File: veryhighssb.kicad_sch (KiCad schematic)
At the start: 1 part, among them U1 STM32WL33CCV6TR

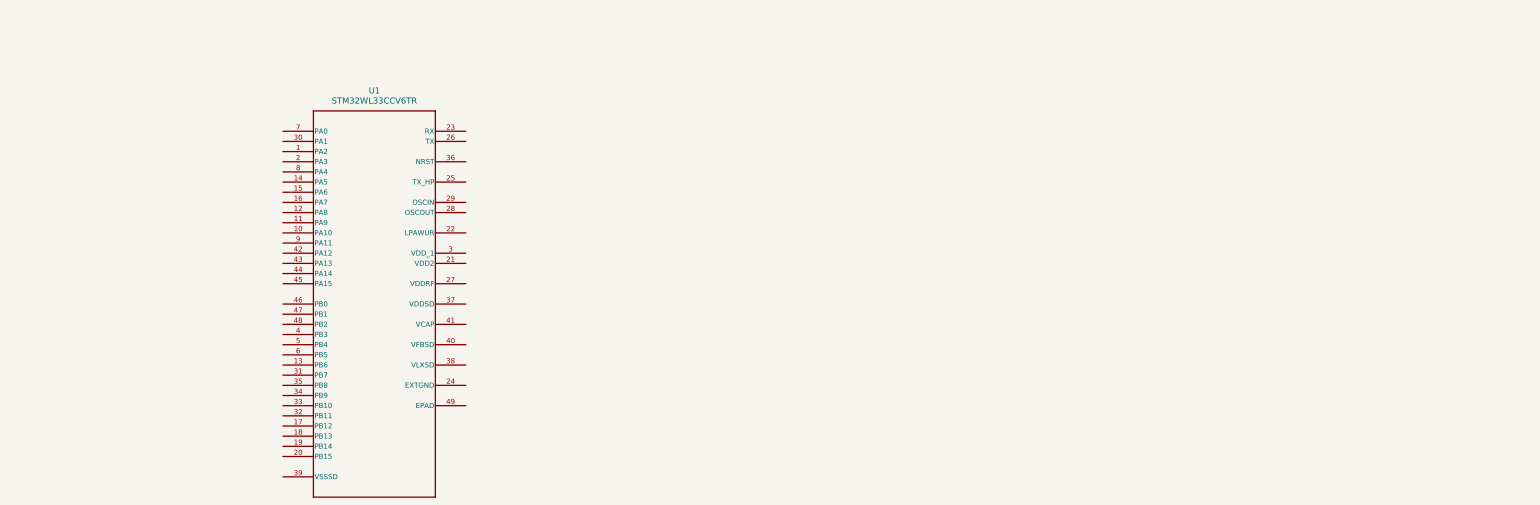
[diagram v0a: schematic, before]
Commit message: Added mcu, swd
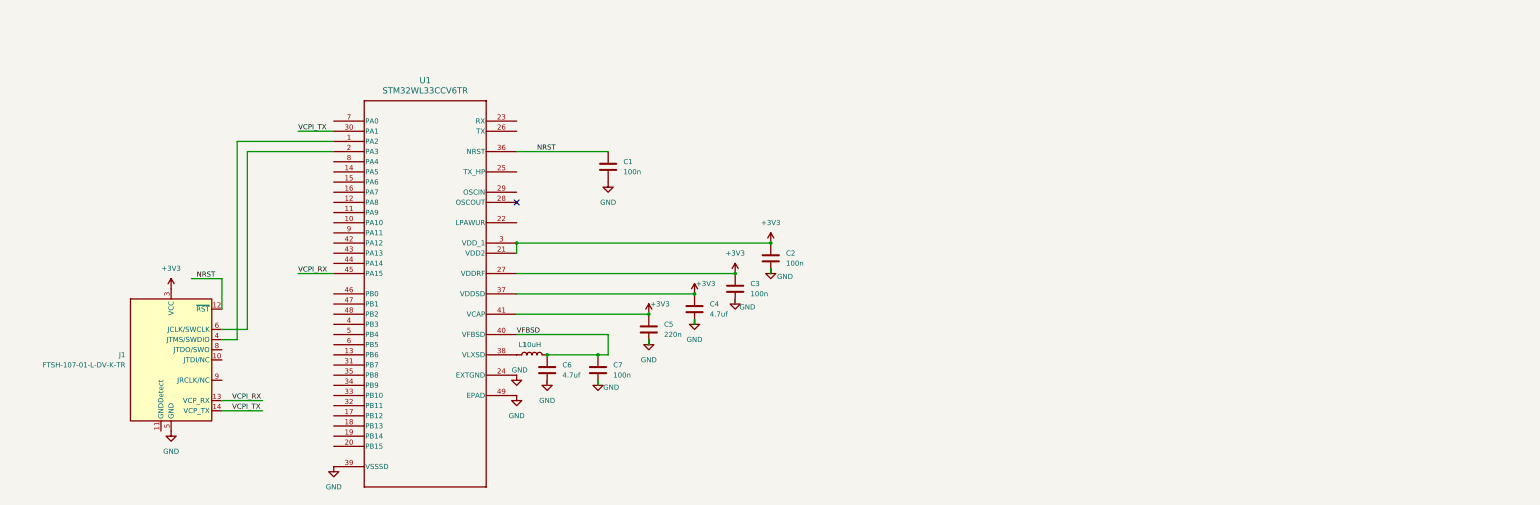
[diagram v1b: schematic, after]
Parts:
- added C1, C2, C3, C7: 100n, Capacitor_SMD:C_0805_2012Metric_Pad1.18x1.45mm_HandSolder, symbol Device:C
- added C4, C6: 4.7uf, Capacitor_SMD:C_0805_2012Metric_Pad1.18x1.45mm_HandSolder, symbol Device:C
- added C5: 220n, Capacitor_SMD:C_0805_2012Metric_Pad1.18x1.45mm_HandSolder, symbol Device:C
- added J1: FTSH-107-01-L-DV-K-TR, Conn ARM 14:CON14_2X7_DUK_FTSH_SAI, symbol Connector:Conn_ST_STDC14
- added L1: 10uH, Inductor_SMD:L_0805_2012Metric_Pad1.05x1.20mm_HandSolder, symbol Device:L
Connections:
- net at U1.1 (PA2): now also J1.4 (JTMS/SWDIO)
- net at U1.2 (PA3): now also J1.6 (JCLK/SWCLK)
- net +3V3: now reaches U1.21 (VDD2)
- net +3V3: now also U1.27 (VDDRF), U1.3 (VDD_1), U1.37 (VDDSD), U1.41 (VCAP), C2.1, C3.1, C4.1, C5.1, J1.3 (VCC)
- net GND: now reaches U1.24 (EXTGND)
- net GND: now also U1.39 (VSSSD), U1.49 (EPAD), C1.2, C2.2, C3.2, C4.2, C5.2, C6.2, C7.2, J1.5 (GND), J1.7 (GND)
- net VCPI_TX: now reaches U1.30 (PA1)
- net VCPI_TX: now also J1.14 (VCP_TX)
- net NRST: now reaches U1.36 (NRST)
- net NRST: now also C1.1, J1.12 (~{RST})
- net at U1.38 (VLXSD): now also L1.1
- net VFBSD: now reaches U1.40 (VFBSD)
- net VFBSD: now also C6.1, C7.1, L1.2
- net VCPI_RX: now reaches U1.45 (PA15)
- net VCPI_RX: now also J1.13 (VCP_RX)
- no-connect marks 0 -> 1
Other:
- moved on the sheet: U1

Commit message: added symbol for TCXO
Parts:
- added C8, C9: 100p, Capacitor_SMD:C_0805_2012Metric_Pad1.18x1.45mm_HandSolder, symbol Device:C
- added U2: XTC4010-1, LocalLibrary:Crystal_SMD_2016-6Pin_2.0x1.6mm, symbol LocalLibrary:XTC4010-1
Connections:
- net +3V3: now also C9.2, U2.4 (VCC)
- net GND: now also C9.1
- net at U1.29 (OSCIN): now also C8.1
- new net: C8.2, U2.3 (OUT)

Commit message: some progress
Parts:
- removed U2: XTC4010-1, LocalLibrary:Crystal_SMD_2016-6Pin_2.0x1.6mm, symbol LocalLibrary:XTC4010-1
- added J2: Conn_01x01_Pin, Connector_PinSocket_2.54mm:PinSocket_1x01_P2.54mm_Vertical, symbol Connector:Conn_01x01_Pin
- added JP1: SolderJumper, Jumper:SolderJumper-2_P1.3mm_Open_Pad1.0x1.5mm, symbol Jumper:SolderJumper_2_Open
- added U2: XTC4010-1, symbol LocalSymbols:XTC4010-1
- C8: value 100p -> 10p
- C9: value 100p -> 10n
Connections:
- net +3V3: now also C9.1, U2.4 (VCC); no longer C9.2
- net GND: now also C9.2, JP1.2 (B), U2.2 (GND); no longer C2.2, C9.1
- net at C8.2: now also U2.3 (OUT)
- net at U1.22 (LPAWUR): now also JP1.1 (A)
- net at U1.28 (OSCOUT): now also J2.1 (Pin_1)
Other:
- moved on the sheet: C1

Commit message: some progress
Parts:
- added C10: 15p, Capacitor_SMD:C_0805_2012Metric_Pad1.18x1.45mm_HandSolder, symbol Device:C
- added C11: 33p, Capacitor_SMD:C_0805_2012Metric_Pad1.18x1.45mm_HandSolder, symbol Device:C
- added C12, C13: DNP, Capacitor_SMD:C_0805_2012Metric_Pad1.18x1.45mm_HandSolder, symbol Device:C
- added L2: 120nH, Inductor_SMD:L_0805_2012Metric_Pad1.05x1.20mm_HandSolder, symbol Device:L
- added L3: DNP, Inductor_THT:L_Axial_L7.0mm_D3.3mm_P12.70mm_Horizontal_Fastron_MICC, symbol Device:L
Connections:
- net RX: now reaches U1.23 (RX)
- net RX: now also C10.1, C13.1, L2.1, L3.1
- new net: C11.1, C12.1, L2.2, L3.2
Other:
- note added: "Input inpedance 169 MHz 176 + j265 PI pad 30 pF 128 nH 14.6 pF"

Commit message: some progress
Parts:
- added JP2, JP3, JP4, JP5: ~, symbol Jumper:Jumper_2_Open
- added L4: 30nH, Inductor_SMD:L_0805_2012Metric_Pad1.05x1.20mm_HandSolder, symbol Device:L
- C10: value 15p -> 96p
- C11: value 33p -> 36p
- C12: value DNP -> 4.7p
- C13: value DNP -> 1000p
- L2: value 120nH -> 240nH
- L3: value DNP -> 11nH; footprint Inductor_THT:L_Axial_L7.0mm_D3.3mm_P12.70mm_Horizontal_Fastron_MICC -> Inductor_SMD:L_0805_2012Metric_Pad1.05x1.20mm_HandSolder
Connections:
- net RX: now also JP2.1 (A); no longer C10.1, C13.1, L2.1, L3.1
- net at C12.1, L2.2: no longer C11.1, L3.2
- net at C12.2: now also C11.1, JP4.1 (A), L4.2
- net at C13.2: now also C10.1, L2.1, L3.2
- new net: C13.1, JP2.2 (B)
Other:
- note added: "Input inpedance 169 MHz 176 + j265 3rd Order Butterworth Bandpass Conventional, Shunt First Lower Cutoff Freq. = 130 MHz; Upper Cutoff Freq. = 180 MHz nmarkimicrowave.com Inductor Q Factor = 30 at 100.0MHz"
- note removed: "Input inpedance 169 MHz 176 + j265 PI pad 30 pF 128 nH 14.6 pF"
- moved on the sheet: C10, C11, L2

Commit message: some progress
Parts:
- added JP6: ~, symbol Jumper:SolderJumper_3_Open
- added Q1: RD15HVF1, Package_TO_SOT_THT:TO-220-3_Horizontal_TabDown, symbol Transistor_FET:Q_NMOS_GSD
- added Q3: RD01MUS2, Package_TO_SOT_SMD:SOT-89-3_Handsoldering, symbol Transistor_FET:Q_NMOS_GSD
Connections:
- net TX HP: now reaches U1.25 (TX_HP)
- net TX HP: now also JP6.1 (A)
- net TX: now reaches U1.26 (TX)
- net TX: now also JP6.3 (B)
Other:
- note added: "https://forum.mountainqrp.it/t/transverter-ur3lmz-ad-alta-dinamica/6375 https://www.qsl.net/in3otd/ham_radio/TRV144_28/TRV144_28.html https://groups.google.com/g/hermes-lite/c/tq0SsZS-HM0/m/vXsSuylXAQAJ"

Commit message: added TX
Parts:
- added C14: 100, symbol Device:C
- added C15, C19, C20, C24, C25, C26: 100n, Capacitor_SMD:C_0805_2012Metric_Pad1.18x1.45mm_HandSolder, symbol Device:C
- added C16, C21: 100p, Capacitor_SMD:C_0805_2012Metric_Pad1.18x1.45mm_HandSolder, symbol Device:C
- added C17, C18, C22, C23: TBD, Capacitor_SMD:C_0805_2012Metric_Pad1.18x1.45mm_HandSolder, symbol Device:C
- added JP7: ~, symbol Jumper:Jumper_2_Open
- added L10, L6, L7, L8, L9: TBD, Inductor_SMD:L_0805_2012Metric_Pad1.05x1.20mm_HandSolder, symbol Device:L
- added L5: 120nH, Inductor_SMD:L_0805_2012Metric_Pad1.05x1.20mm_HandSolder, symbol Device:L
- added R1, R5: 100, symbol Device:R
- added R2: 5k6, symbol Device:R
- added R3, R6: 2k2, symbol Device:R
- added R4: 1, symbol Device:R
- added R7: 3k3, symbol Device:R
- added RV1: 1k, symbol Device:R_Potentiometer_Small
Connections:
- net VFBSD: now also C15.1, C16.1, L5.2
- net at Q1.1 (G): now also C23.1, L8.1, R5.2
- net at Q1.3 (D): now also L9.2
- net at JP6.2 (C): now also C14.1, L5.1
- net at Q3.1 (G): now also C18.1, L6.1, R1.2
- net at Q3.3 (D): now also C21.1, L7.2
- new net: C26.1, JP7.1 (A), L10.1
- new net: C20.1, L7.1, R4.2
- new net: C19.1, R1.1, R2.2, R3.1
- new net: C14.2, C17.1, L6.2
- new net: R6.1, RV1.1
- new net: C25.1, L10.2, L9.1
- new net: R7.2, RV1.3
- new net: C24.1, R5.1, RV1.2
- new net: C21.2, C22.1, L8.2
- new net +12: R4.1
- new net 8V-TX: R2.1, R7.1
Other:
- moved on the sheet: JP6, Q1, Q3
